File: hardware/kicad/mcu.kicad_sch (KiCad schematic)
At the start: 11 parts, among them CN1 OLED_SSD1306_I2C, SW1 RESET, SW2 BOOT, U6 ESP32-S3-WROOM-1-N16R8

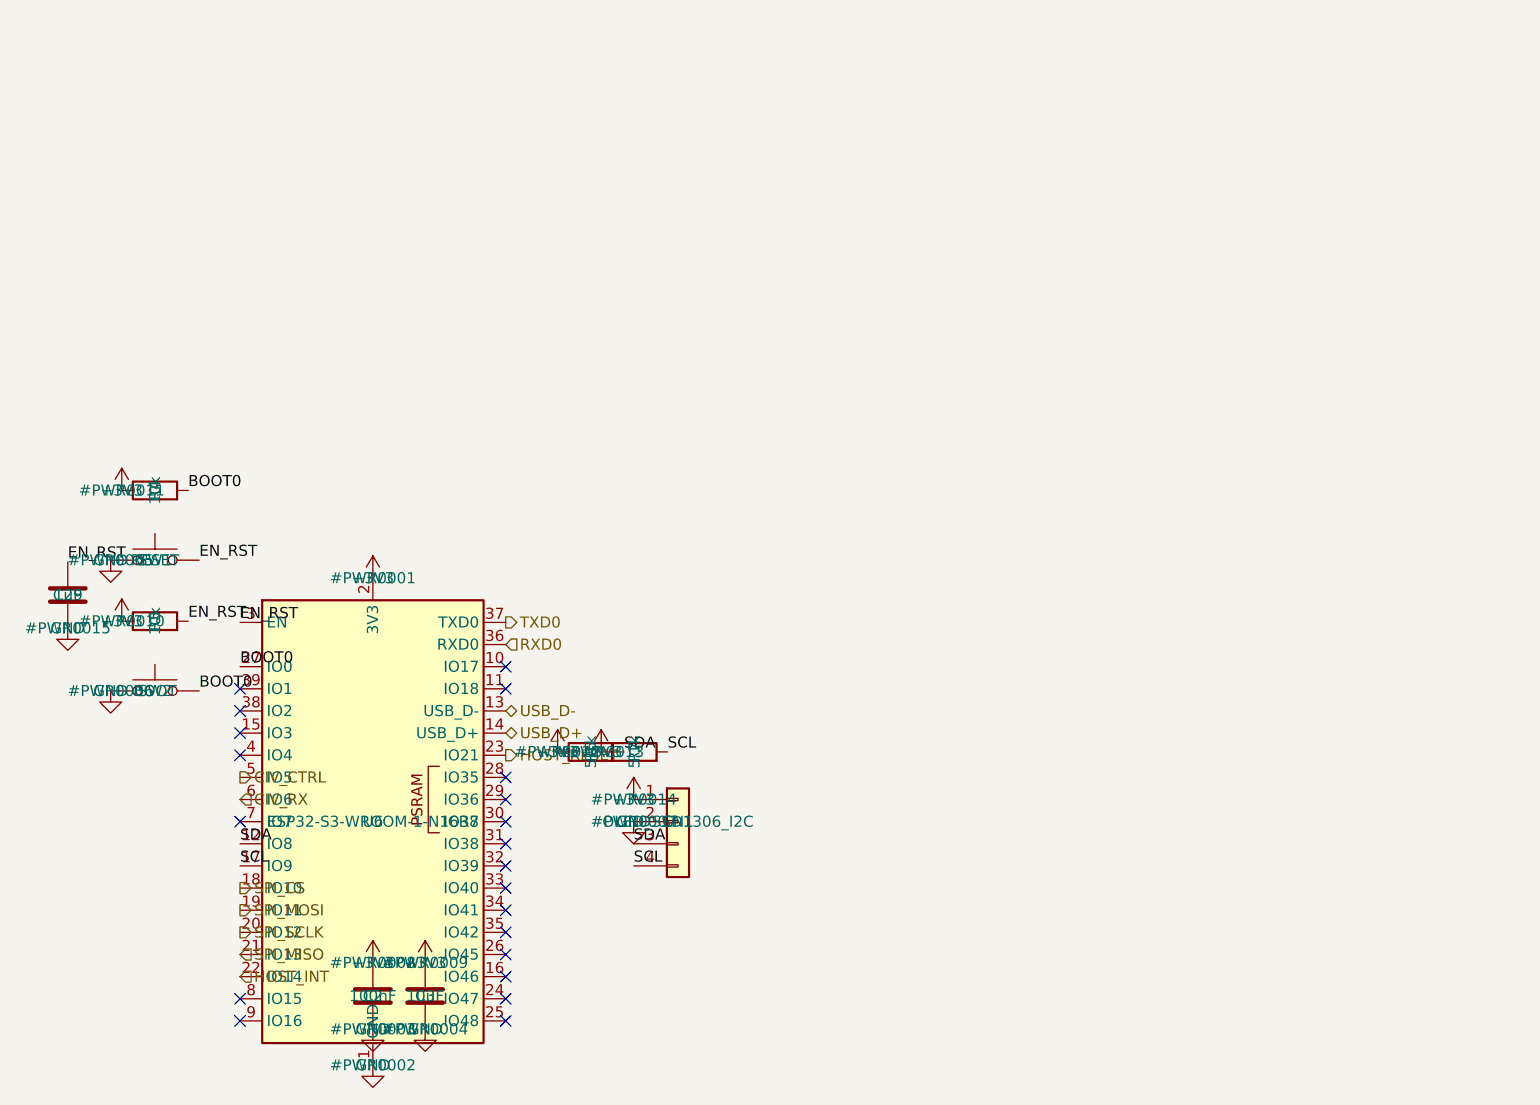
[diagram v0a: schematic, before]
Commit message: Refactor the microcontroller sheet; add switch footprint and 3d file; add titles, date and WaveRig annotation to all sheets.
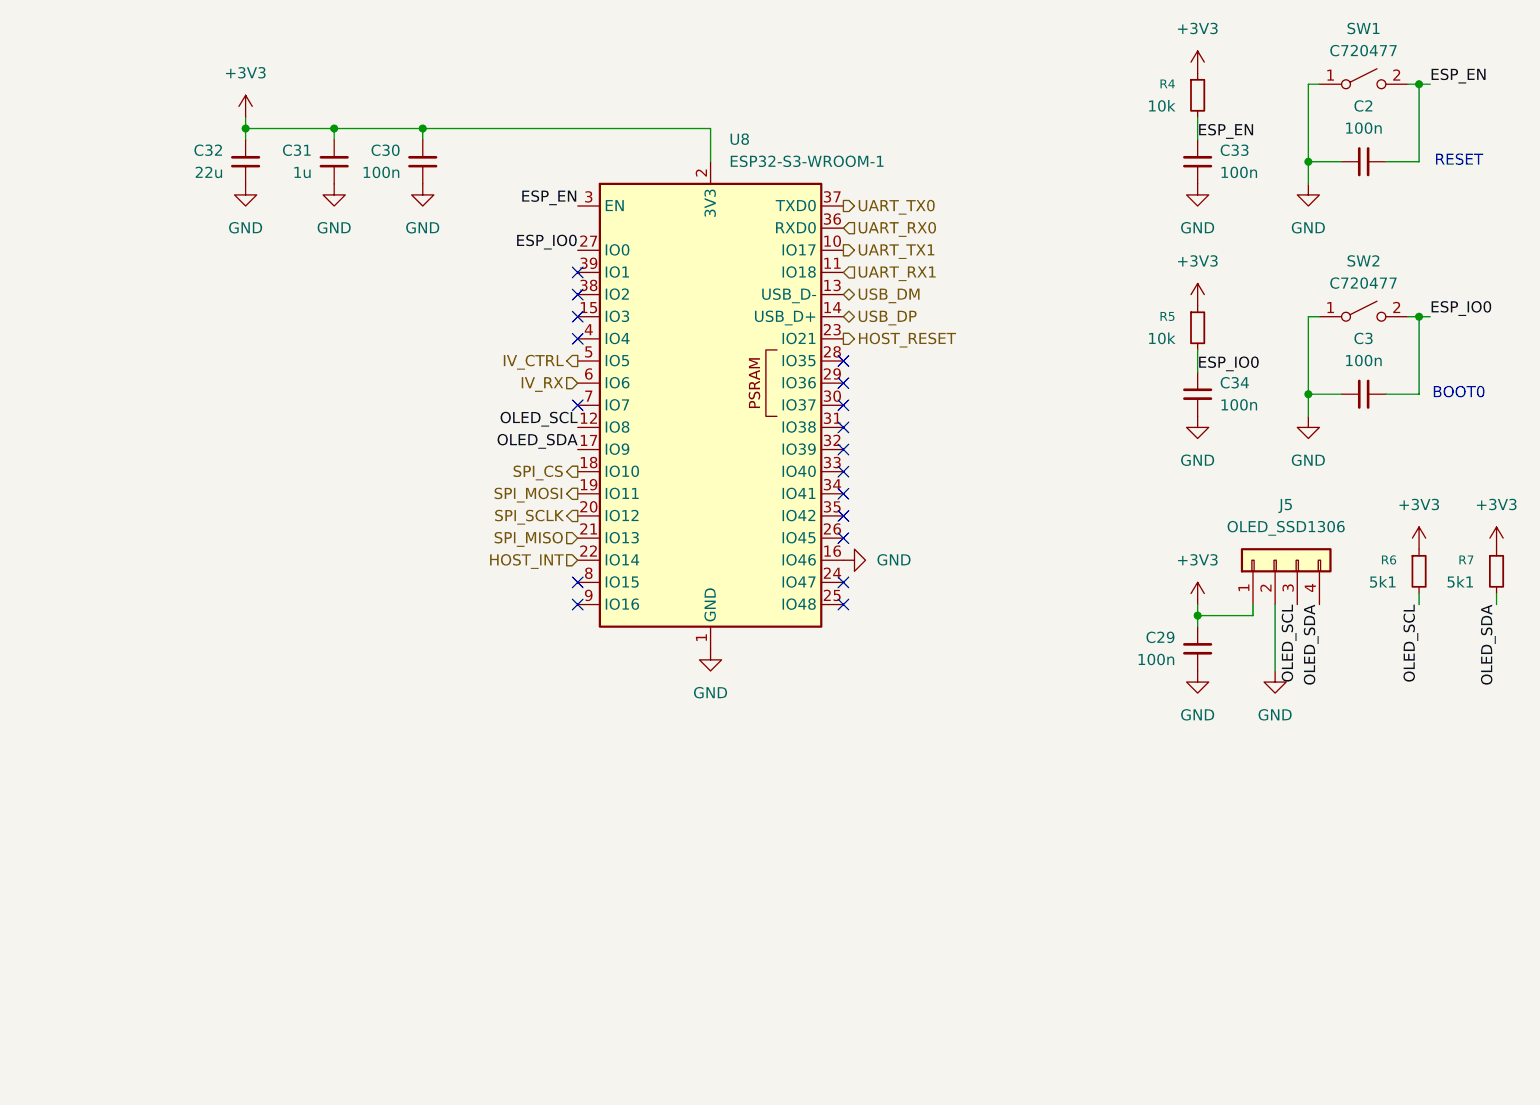
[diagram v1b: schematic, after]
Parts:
- removed C2: 100nF, Capacitor_SMD:C_0603_1608Metric, symbol Device:C
- removed C29: 1uF, Capacitor_SMD:C_0603_1608Metric, symbol Device:C
- removed C3: 10uF, Capacitor_SMD:C_0603_1608Metric, symbol Device:C
- removed CN1: OLED_SSD1306_I2C, Connector_JST:JST_PH_B4B-PH-K_1x04_P2.00mm_Vertical, symbol Connector_Generic:Conn_01x04
- removed R4, R5: 10k, Resistor_SMD:R_0603_1608Metric, symbol Device:R
- removed R6, R7: 5.1k, Resistor_SMD:R_0603_1608Metric, symbol Device:R
- removed SW1: RESET, Button_Switch_SMD:SW_SPST_B3S-1000, symbol Switch:SW_Push
- removed SW2: BOOT, Button_Switch_SMD:SW_SPST_B3S-1000, symbol Switch:SW_Push
- removed U6: ESP32-S3-WROOM-1-N16R8, RF_Module:ESP32-S3-WROOM-1, symbol RF_Module:ESP32-S3-WROOM-1
- added C2, C29, C3, C30, C33, C34: 100n, Capacitor_SMD:C_0603_1608Metric, symbol Device:C_Small
- added C31: 1u, Capacitor_SMD:C_0603_1608Metric, symbol Device:C_Small
- added C32: 22u, Capacitor_SMD:C_0603_1608Metric, symbol Device:C_Small
- added J5: OLED_SSD1306, Connector_PinHeader_2.54mm:PinHeader_1x04_P2.54mm_Vertical, symbol Connector_Generic:Conn_01x04
- added R4, R5: 10k, Resistor_SMD:R_0603_1608Metric, symbol Device:R_Small
- added R6, R7: 5k1, Resistor_SMD:R_0603_1608Metric, symbol Device:R_Small
- added SW1, SW2: C720477, WaveRig_Custom:SW-SMD_L3.9-W3.0-P4.45, symbol Switch:SW_SPST
- added U8: ESP32-S3-WROOM-1, RF_Module:ESP32-S3-WROOM-1, symbol RF_Module:ESP32-S3-WROOM-1
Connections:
- net +3V3: now also C29.2, C30.2, C31.2, C32.2, J5.1 (Pin_1), R4.1, R5.1, R6.1, R7.1, U8.2 (3V3)
- net GND: now also C2.1, C29.1, C3.1, C30.1, C31.1, C32.1, C33.1, C34.1, J5.2 (Pin_2), SW1.1 (A), SW2.1 (A), U8.1 (GND), U8.16 (IO46), U8.40 (GND), U8.41 (GND)
- net HOST_INT: now also U8.22 (IO14)
- net HOST_RESET: now also U8.23 (IO21)
- net SPI_CS: now also U8.18 (IO10)
- net SPI_MISO: now also U8.21 (IO13)
- net SPI_MOSI: now also U8.19 (IO11)
- net SPI_SCLK: now also U8.20 (IO12)
- new net ESP_EN: C2.2, C33.2, R4.2, SW1.2 (B), U8.3 (EN)
- new net ESP_IO0: C3.2, C34.2, R5.2, SW2.2 (B), U8.27 (IO0)
- new net IV_CTRL: U8.5 (IO5)
- new net IV_RX: U8.6 (IO6)
- new net OLED_SCL: J5.3 (Pin_3), R6.2, U8.12 (IO8)
- new net OLED_SDA: J5.4 (Pin_4), R7.2, U8.17 (IO9)
- new net UART_RX0: U8.36 (RXD0)
- new net UART_RX1: U8.11 (IO18)
- new net UART_TX0: U8.37 (TXD0)
- new net UART_TX1: U8.10 (IO17)
- new net USB_DM: U8.13 (USB_D-)
- new net USB_DP: U8.14 (USB_D+)
- no-connect marks 21 -> 18
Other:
- note added: "BOOT0"
- note added: "RESET"
- company: (none) -> WaveRig
- title: (none) -> Microcontroller Sheet
